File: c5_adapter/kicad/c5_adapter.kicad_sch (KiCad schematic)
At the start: 8 parts, among them IC1 TLV6700DDCR, J1 Conn_01x10, J2 Conn_01x10, SW1 SW_DPDT_x2, SW2 SW_DPDT_x2, U1 ESP32-C5-DevKitC-1

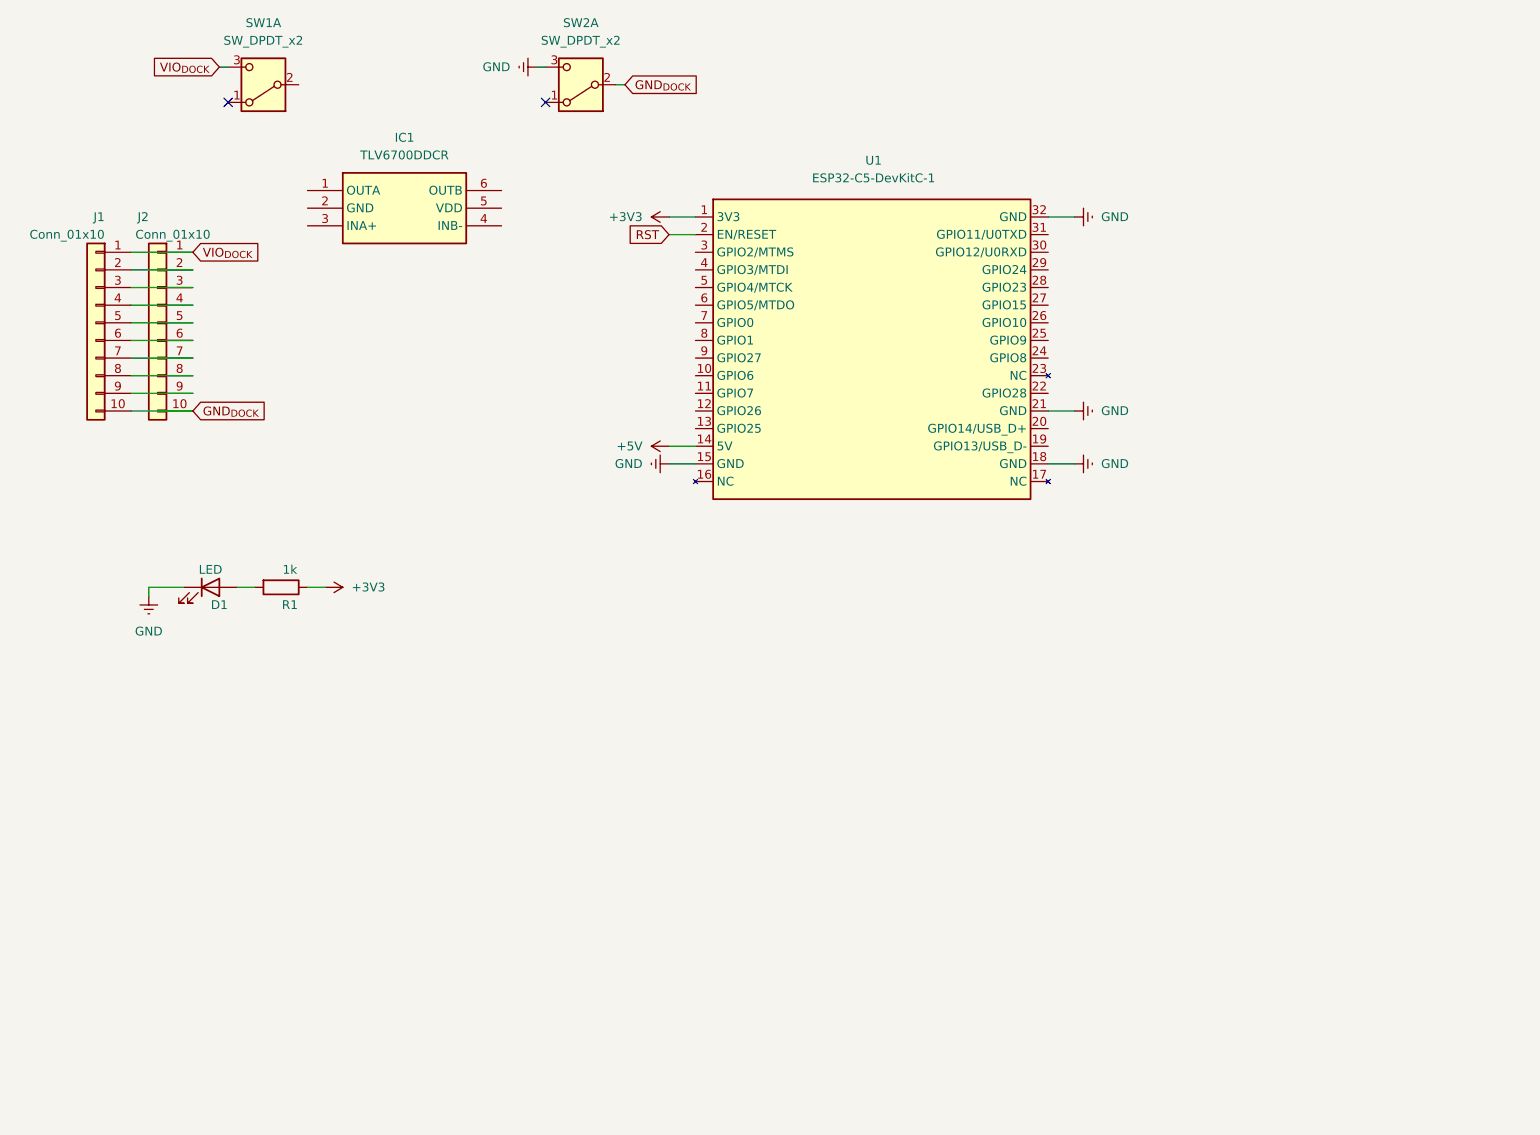
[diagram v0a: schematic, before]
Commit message: Updated C5 schematic
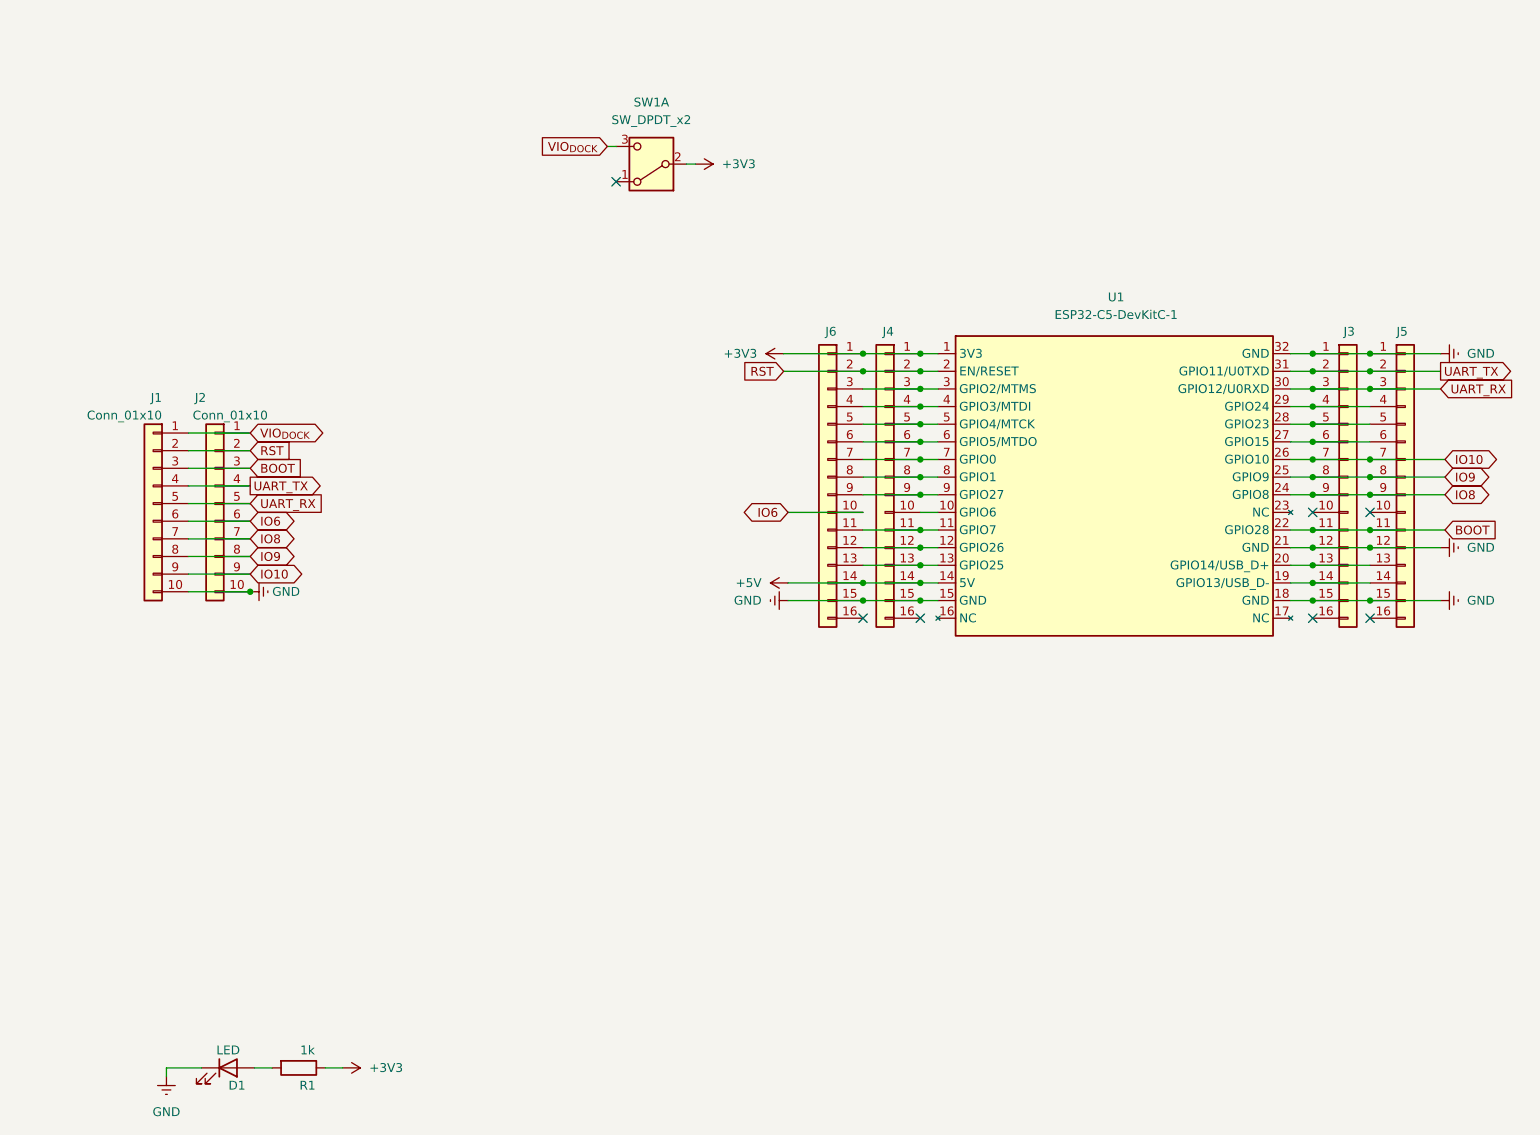
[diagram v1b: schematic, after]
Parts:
- removed IC1: TLV6700DDCR, TLV6700DDCR:SOT95P280X110-6N, symbol TLV6700DDCR:TLV6700DDCR
- removed SW2: SW_DPDT_x2, symbol Switch:SW_DPDT_x2
- added J3, J4: Conn_01x16, Connector_PinSocket_2.54mm:PinSocket_1x16_P2.54mm_Vertical, symbol Connector_Generic:Conn_01x16
- added J5, J6: Conn_01x16, Connector_PinHeader_2.54mm:PinHeader_1x16_P2.54mm_Vertical, symbol Connector_Generic:Conn_01x16
- U1: now left out of the parts list
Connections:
- net GND_{DOCK} is gone; now on net GND: J1.10 (Pin_10), J2.10 (Pin_10)
- net +3V3: now also SW1.2 (B), J4.1 (Pin_1), J6.1 (Pin_1)
- net +5V: now also J4.14 (Pin_14), J6.14 (Pin_14)
- net GND: now also J3.1 (Pin_1), J3.12 (Pin_12), J3.15 (Pin_15), J4.15 (Pin_15), J5.1 (Pin_1), J5.12 (Pin_12), J5.15 (Pin_15), J6.15 (Pin_15)
- net RST: now also J1.2 (Pin_2), J2.2 (Pin_2), J4.2 (Pin_2), J6.2 (Pin_2)
- net BOOT: now reaches J1.3 (Pin_3), J2.3 (Pin_3)
- net BOOT: now also U1.22 (GPIO28), J3.11 (Pin_11), J5.11 (Pin_11)
- net UART_TX: now reaches J1.4 (Pin_4), J2.4 (Pin_4)
- net UART_TX: now also U1.31 (GPIO11/U0TXD), J3.2 (Pin_2), J5.2 (Pin_2)
- net UART_RX: now reaches J1.5 (Pin_5), J2.5 (Pin_5)
- net UART_RX: now also U1.30 (GPIO12/U0RXD), J3.3 (Pin_3), J5.3 (Pin_3)
- net IO6: now reaches J1.6 (Pin_6), J2.6 (Pin_6)
- net IO6: now also J6.10 (Pin_10)
- net IO8: now reaches J1.7 (Pin_7), J2.7 (Pin_7)
- net IO8: now also U1.24 (GPIO8), J3.9 (Pin_9), J5.9 (Pin_9)
- net IO9: now reaches J1.8 (Pin_8), J2.8 (Pin_8)
- net IO9: now also U1.25 (GPIO9), J3.8 (Pin_8), J5.8 (Pin_8)
- net IO10: now reaches J1.9 (Pin_9), J2.9 (Pin_9)
- net IO10: now also U1.26 (GPIO10), J3.7 (Pin_7), J5.7 (Pin_7)
- net at U1.10 (GPIO6): now also J4.10 (Pin_10)
- net at U1.11 (GPIO7): now also J4.11 (Pin_11), J6.11 (Pin_11)
- net at U1.12 (GPIO26): now also J4.12 (Pin_12), J6.12 (Pin_12)
- net at U1.13 (GPIO25): now also J4.13 (Pin_13), J6.13 (Pin_13)
- net at U1.19 (GPIO13/USB_D-): now also J3.14 (Pin_14), J5.14 (Pin_14)
- net at U1.20 (GPIO14/USB_D+): now also J3.13 (Pin_13), J5.13 (Pin_13)
- net at U1.27 (GPIO15): now also J3.6 (Pin_6), J5.6 (Pin_6)
- net at U1.28 (GPIO23): now also J3.5 (Pin_5), J5.5 (Pin_5)
- net at U1.29 (GPIO24): now also J3.4 (Pin_4), J5.4 (Pin_4)
- net at U1.3 (GPIO2/MTMS): now also J4.3 (Pin_3), J6.3 (Pin_3)
- net at U1.4 (GPIO3/MTDI): now also J4.4 (Pin_4), J6.4 (Pin_4)
- net at U1.5 (GPIO4/MTCK): now also J4.5 (Pin_5), J6.5 (Pin_5)
- net at U1.6 (GPIO5/MTDO): now also J4.6 (Pin_6), J6.6 (Pin_6)
- net at U1.7 (GPIO0): now also J4.7 (Pin_7), J6.7 (Pin_7)
- net at U1.8 (GPIO1): now also J4.8 (Pin_8), J6.8 (Pin_8)
- net at U1.9 (GPIO27): now also J4.9 (Pin_9), J6.9 (Pin_9)
- no-connect marks 2 -> 7
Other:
- moved on the sheet: D1, J1, J2, R1, SW1A, U1

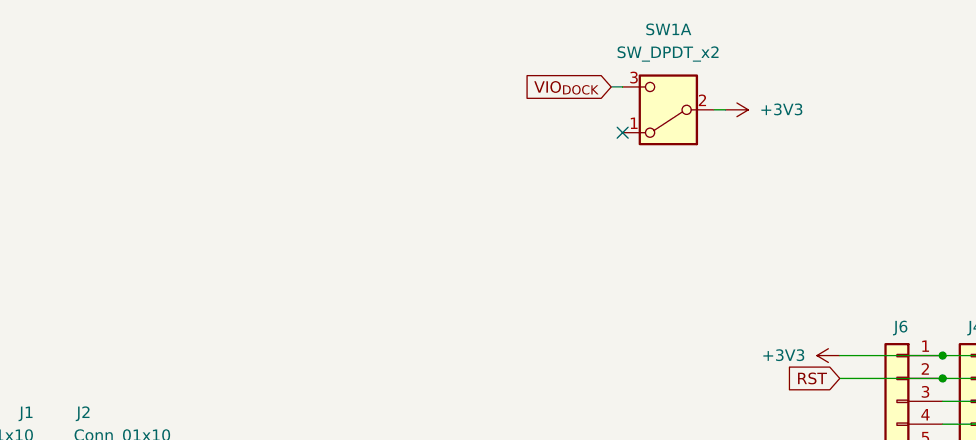
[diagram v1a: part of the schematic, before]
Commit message: Added SPDT switch
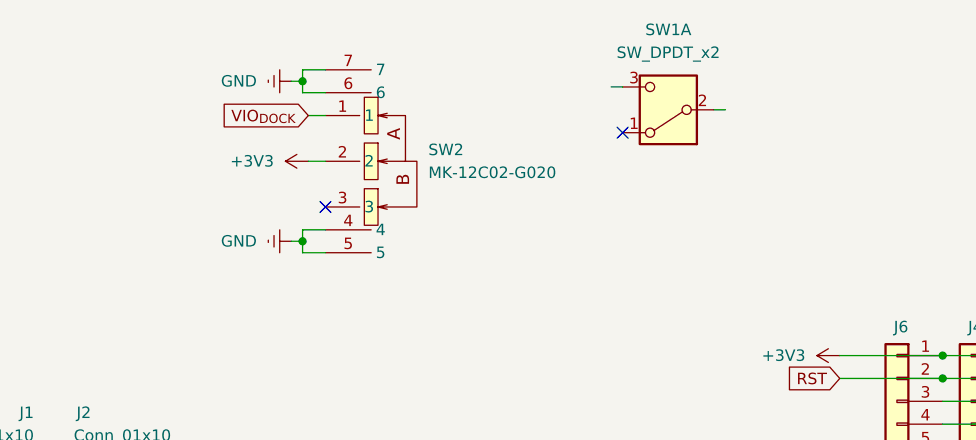
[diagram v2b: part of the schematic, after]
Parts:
- added SW2: MK-12C02-G020, C5-Addon:SW-SMD_MK-12C02-G020, symbol C5-Addon:MK-12C02-G020
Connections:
- net +3V3: now also SW2.2; no longer SW1.2 (B)
- net GND: now also SW2.4, SW2.5, SW2.6, SW2.7
- net VIO_{DOCK}: now also SW2.1; no longer SW1.3 (C)
- no-connect marks 7 -> 8

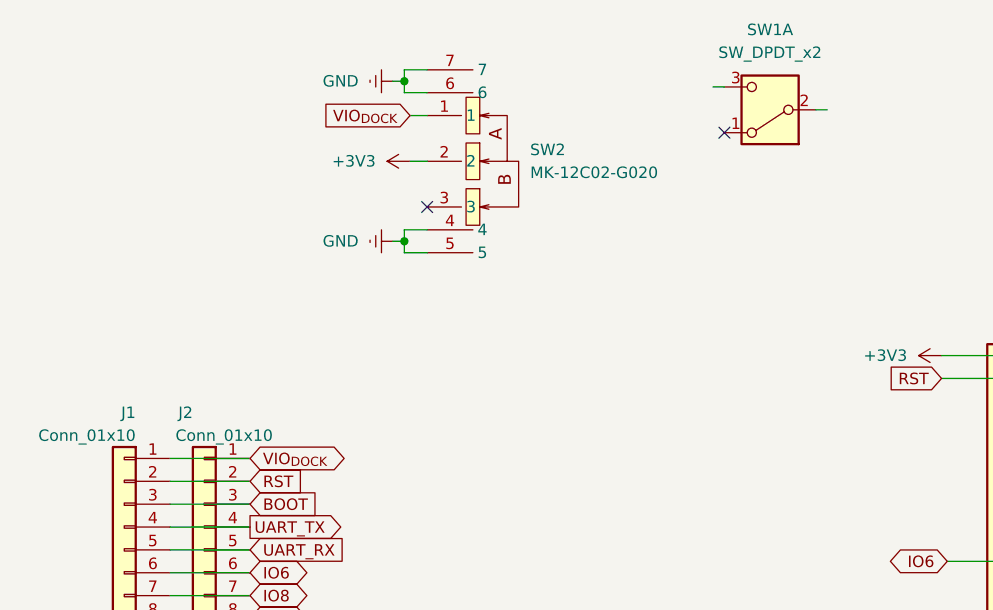
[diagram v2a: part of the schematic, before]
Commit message: Initial PCB placement
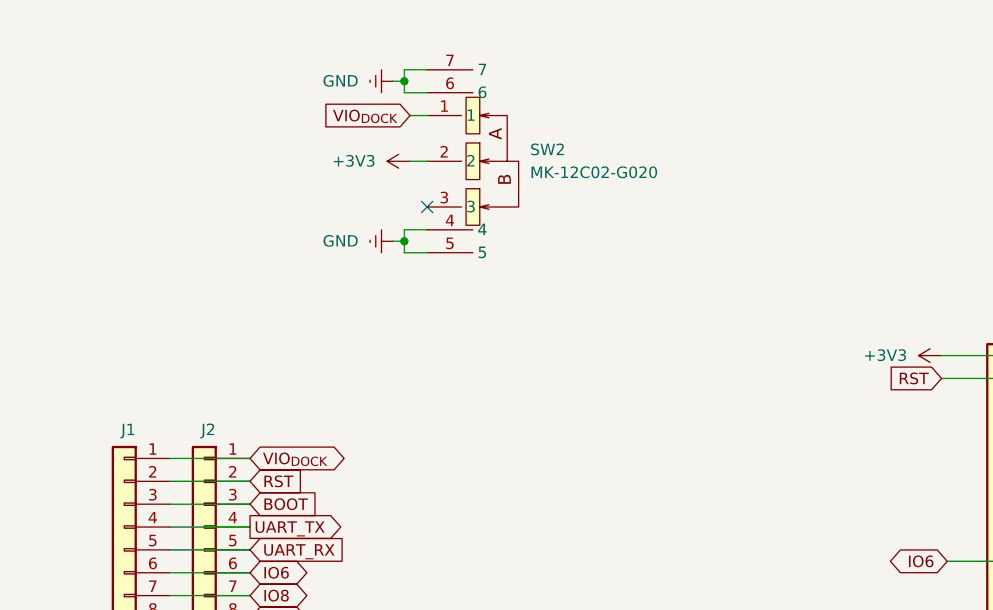
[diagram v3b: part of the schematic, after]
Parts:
- removed SW1: SW_DPDT_x2, symbol Switch:SW_DPDT_x2
- J1: footprint pinheader-reduced:PinHeader_1x10_P2.54mm_Vertical_Reduced_2 -> Connector_PinSocket_2.54mm:PinSocket_1x10_P2.54mm_Horizontal
- J2: footprint Connector_PinSocket_2.54mm:PinSocket_1x10_P2.54mm_Horizontal -> Connector_PinSocket_2.54mm:PinSocket_1x10_P2.54mm_Vertical; now left out of the parts list
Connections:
- no-connect marks 8 -> 7
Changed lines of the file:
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@@
 	)
 	(no_connect
-		(at 125.73 48.26)
-	)
-	(no_connect
 		(at 234.315 111.125)
 	)
@@
 	(wire
 		(pts
-			(xy 124.46 43.18) (xy 125.73 43.18)
-		)
-		(stroke
-			(width 0)
-			(type default)
-		)
-	)
-	(wire
-		(pts
 			(xy 90.17 61.595) (xy 92.71 61.595)
 		)
@@
 	(wire
 		(pts
-			(xy 137.16 45.72) (xy 135.89 45.72)
-		)
-		(stroke
-			(width 0)
-			(type default)
-		)
-	)
-	(wire
-		(pts
 			(xy 64.135 94.615) (xy 73.025 94.615)
 		)
@@
 	)
 	(symbol
-		(lib_id "Switch:SW_DPDT_x2")
-		(at 130.81 45.72 180)
-		(unit 1)
-		(body_style 1)
-		(exclude_from_sim no)
-		(in_bom yes)
-		(on_board yes)
-		(in_pos_files yes)
-		(dnp no)
-		(fields_autoplaced yes)
-		(property "Reference" "SW1"
-			(at 130.81 36.83 0)
-			(show_name no)
-			(do_not_autoplace no)
-			(effects
-				(font
-					(size 1.27 1.27)
-				)
-			)
-		)
-		(property "Value" "SW_DPDT_x2"
-			(at 130.81 39.37 0)
-			(show_name no)
-			(do_not_autoplace no)
-			(effects
-				(font
-					(size 1.27 1.27)
-				)
-			)
-		)
-		(property "Footprint" ""
-			(at 130.81 45.72 0)
-			(hide yes)
-			(show_name no)
-			(do_not_autoplace no)
-			(effects
-				(font
-					(size 1.27 1.27)
-				)
-			)
-		)
-		(property "Datasheet" ""
-			(at 130.81 45.72 0)
-			(hide yes)
-			(show_name no)
-			(do_not_autoplace no)
-			(effects
-				(font
-					(size 1.27 1.27)
-				)
-			)
-		)
-		(property "Description" "Switch, dual pole double throw, separate symbols"
-			(at 130.81 45.72 0)
-			(hide yes)
-			(show_name no)
-			(do_not_autoplace no)
-			(effects
-				(font
-					(size 1.27 1.27)
-				)
-			)
-		)
-		(pin "6"
-		)
-		(pin "1"
-		)
-		(pin "2"
-		)
-		(pin "3"
-		)
-		(pin "4"
-		)
-		(pin "5"
-		)
-		(instances
-			(project "c5_adapter"
-				(path "/4ea9e048-096c-4569-98b9-ff311a85c85d"
-					(reference "SW1")
-					(unit 1)
-				)
-			)
-		)
-	)
-	(symbol
 		(lib_id "Connector_Generic:Conn_01x10")
 		(at 67.945 94.615 0)
@@
 		(body_style 1)
 		(exclude_from_sim no)
-		(in_bom yes)
-		(on_board yes)
-		(in_pos_files yes)
+		(in_bom no)
+		(on_board no)
+		(in_pos_files no)
 		(dnp no)
 		(property "Reference" "J2"
-			(at 66.675 79.375 0)
+			(at 69.215 81.28 0)
 			(show_name no)
 			(do_not_autoplace no)
@@
 		(property "Value" "Conn_01x10"
 			(at 75.565 81.915 0)
+			(hide yes)
 			(show_name no)
 			(do_not_autoplace no)
@@
 			)
 		)
-		(property "Footprint" "Connector_PinSocket_2.54mm:PinSocket_1x10_P2.54mm_Horizontal"
+		(property "Footprint" "Connector_PinSocket_2.54mm:PinSocket_1x10_P2.54mm_Vertical"
 			(at 67.945 94.615 0)
 			(hide yes)
@@
 		(dnp no)
 		(property "Reference" "J1"
-			(at 60.325 79.375 0)
+			(at 60.325 81.28 0)
 			(show_name no)
 			(do_not_autoplace no)
@@
 		(property "Value" "Conn_01x10"
 			(at 60.325 81.915 0)
+			(hide yes)
 			(show_name no)
 			(do_not_autoplace no)
@@
 			)
 		)
-		(property "Footprint" "pinheader-reduced:PinHeader_1x10_P2.54mm_Vertical_Reduced_2"
+		(property "Footprint" "Connector_PinSocket_2.54mm:PinSocket_1x10_P2.54mm_Horizontal"
 			(at 59.055 94.615 0)
 			(hide yes)

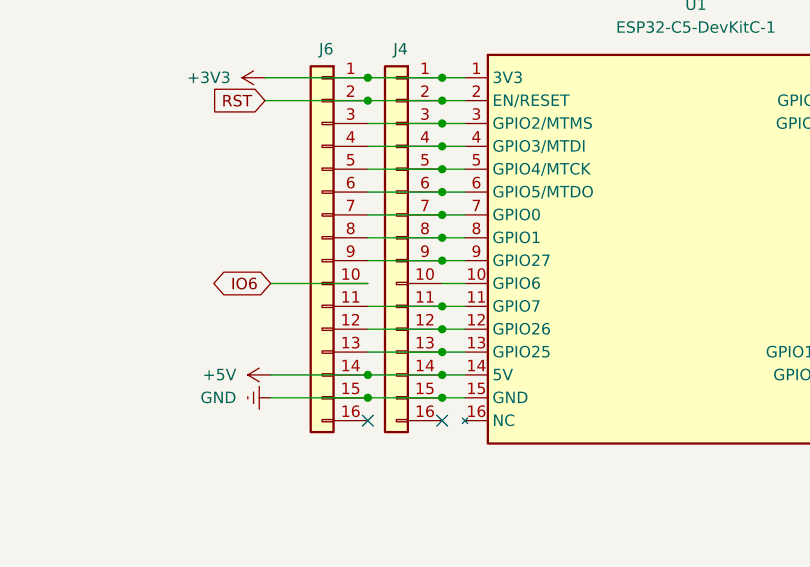
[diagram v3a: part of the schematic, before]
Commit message: Updated c5 adapter PCB placement
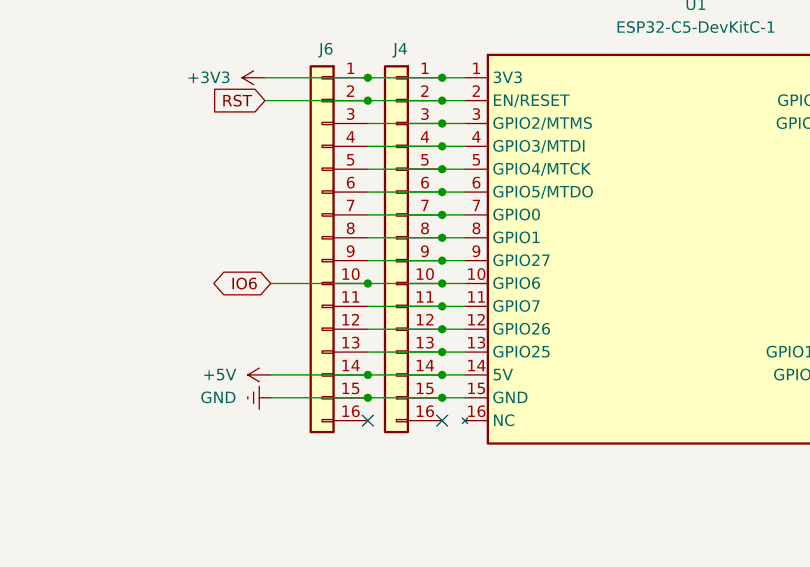
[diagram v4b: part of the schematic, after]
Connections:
- net IO6: now also J4.10 (Pin_10), U1.10 (GPIO6)
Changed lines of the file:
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@@
+	)
+	(junction
+		(at 169.545 95.885)
+		(diameter 0)
+		(color 0 0 0 0)
 	)
 	(junction
@@
 	(junction
 		(at 234.315 108.585)
+		(diameter 0)
+		(color 0 0 0 0)
+	)
+	(junction
+		(at 161.29 95.885)
 		(diameter 0)
 		(color 0 0 0 0)
@@
 		)
 		(stroke
+			(width 0)
+			(type default)
+		)
+	)
+	(wire
+		(pts
+			(xy 161.29 95.885) (xy 169.545 95.885)
+		)
+		(stroke
